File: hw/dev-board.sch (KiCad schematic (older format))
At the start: 8 parts

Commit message: Complete Header connections and internal U2-328 connections. Power regulation and misc passives are up next.
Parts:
- added 100n (x2), 1u: C, symbol C
- added 10K, 1K (x3), R? (x3): R, symbol R
- added D? (x2): LED, symbol LED
- added P?: CONN_02X03, symbol CONN_02X03
- added X?: RESONATOR, symbol RESONATOR
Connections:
- net labels added: +5V, AD0, AD1, AD2, AD3, AD4/SCL, AD4/SDA, AD5/SCL, AREF, IO0/RX, IO1/TX, IO2, IO3, IO4, IO5, IO6, IO7, IO8, IO9, MISO_328, MOSI_328, RES1, RES2, RST_328, RXLED, SCK_328, TXLED, UNUSED, ~SS~_328
- wire segments 5 -> 35
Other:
- moved on the sheet: P?

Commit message: Missing regulators. Xtal is fixed. 3.3v done. Power rails organized.
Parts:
- added C?: 100n, symbol C
- added C?: 470p, symbol C
- added C?: 1u, symbol C
- added CG0603MLC-05E, VR?: VR, symbol VR
- added F?: 500m, symbol F_Small
- added L?: Inductor, symbol L_Small
- added Q?: FDN340P, TO_SOT_Packages_SMD:SOT-23, symbol FDN340P
- added R? (x2): R, symbol R
- added U?: LM358, symbol LM358
- added U?: MIC5205, symbol MIC5205
- added X?: RESONATOR, symbol RESONATOR
- C?: renamed from 100n; value C -> 100n
- C?: renamed from 1u; value C -> 1u
- R?: renamed from 10K; value R -> 10K
- R?: value R -> 10K
- R?: renamed from 1K; value R -> 1K
- renumbered 1K to R?
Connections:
- net labels added: +3.3V, RES1_U2, RES2_U2, USBVCC, VIN
- wire segments 35 -> 59
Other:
- moved on the sheet: P?, R?, X?

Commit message: Add 5V regulator, clean up SOT-223 footprint, created 5V reg schematic symbol
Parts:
- added C?: 100n, symbol C
- added C?: 47u, symbol CP
- added R? (x2): 22R, symbol R
- added U?: LM2940LD-5.0, pcbfp_lib:SOT-223, symbol LM2940LD-5.0
- gave numbers to parts that had none: 1
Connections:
- net labels added: RES1_328, RES2_328
- net labels removed: RES1, RES2
- wire segments 59 -> 64
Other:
- moved on the sheet: C?, P?, Q?, R?, U?, U?A, X?

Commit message: Add schematic drawing of 328PB
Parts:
- added C? (x2): 15pf, symbol C
- added R?: 1M, symbol R
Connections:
- wire segments 64 -> 71
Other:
- moved on the sheet: C?, P?, Q?, R?, U?, U?A

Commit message: Added ATTINY85 schematic and SRAM schematic. Added T1's programming header. Up next, T1 needs a bus switch and everything needs to be duplcated for T2.
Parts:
- removed U?: ATMEGA328P-M, MLF/QFN32, symbol ATMEGA328P-M
- added IC?: ATMEGA328PB-MU, MLF/QFN32, symbol ATMEGA328PB-MU
- added IC?: ATTINY85-SUR, SO8-200, symbol ATTINY85-SUR
- added IC?: 23K256, SMD_Packages:SOIC-8-N, symbol 23K256
- added P? (x2): CONN_02X03, symbol CONN_02X03
- added R?: 10K, symbol R
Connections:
- net labels added: IO3_T1, IO4_T1, MISO_T1, MOSI_T1, SCK_T1, ~RST~_T1
- wire segments 71 -> 80
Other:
- moved on the sheet: C?, P?, R?, X?

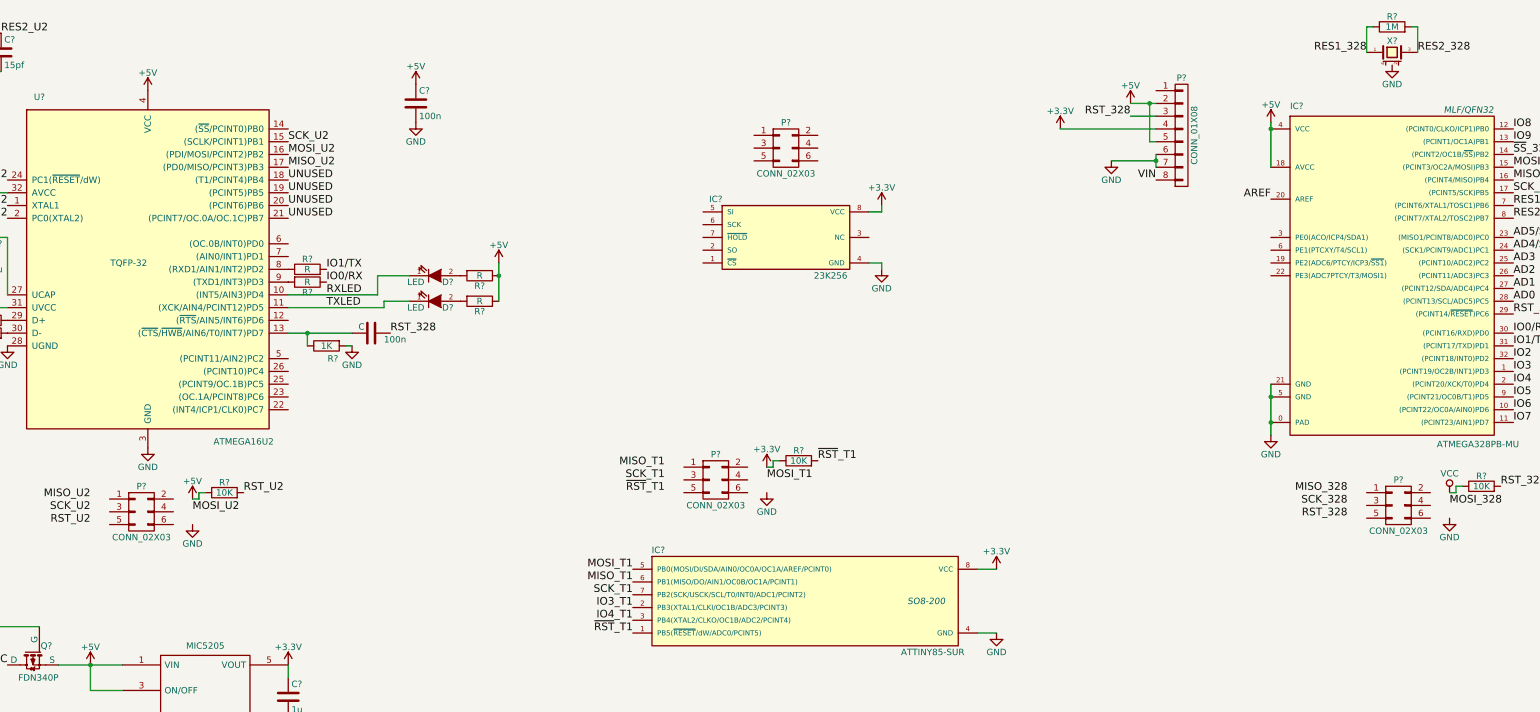
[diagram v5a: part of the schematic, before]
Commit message: Added Bus switch schematic, added a mosfet for power to ram and bs. Needed for programming. BS and ram are not 5v tolerant.
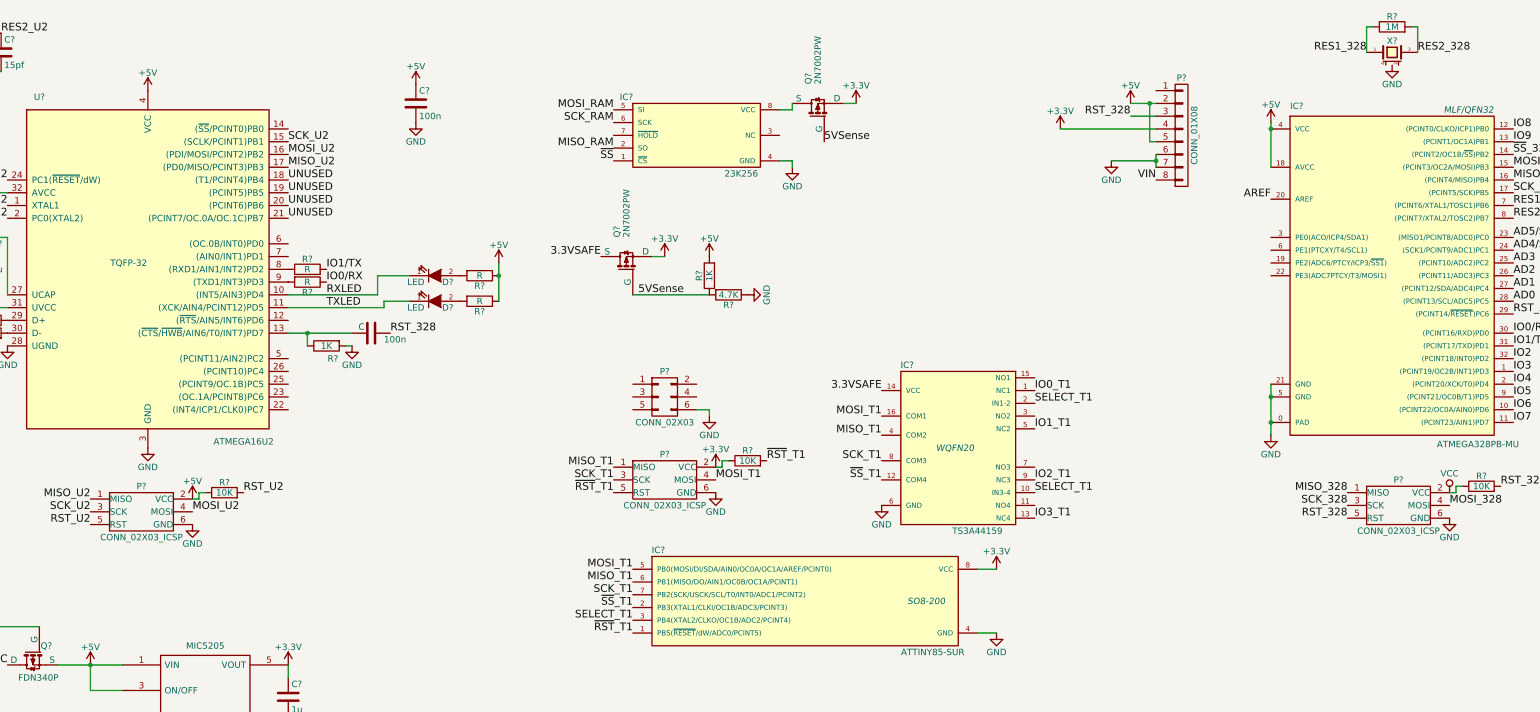
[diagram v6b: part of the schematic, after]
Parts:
- removed P? (x4): CONN_02X03, symbol CONN_02X03
- added IC?: TS3A44159, WQFN20, symbol TS3A44159
- added P? (x3): CONN_02X03_ICSP, symbol CONN_02X03_ICSP
- added P?: CONN_02X03, symbol CONN_02X03
- added Q? (x2): 2N7002PW, TO_SOT_Packages_SMD:SOT-23, symbol 2N7002PW
- added R?: 1K, symbol R
- added R?: 4.7K, symbol R
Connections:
- net +3V3: now also P?.2 (VCC), Q?.~ (S), Q?.~ (S); no longer IC?.8 (VCC)
- net +5V: now also P?.2 (VCC), R?.2
- net GND: now also IC?.6 (GND), P?.6 (GND), P?.6 (GND), P?.6 (GND), P?.6 (P6), R?.1
- net IO3_T1: now also IC?.13 (NC4); no longer IC?.2 (PB3(XTAL1/CLKI/OC1B/ADC3/PCINT3))
- net MISO_328: now also P?.1 (MISO)
- net MISO_T1: now also IC?.4 (COM2), P?.1 (MISO)
- net MISO_U2: now also P?.1 (MISO)
- net MOSI_328: now also P?.4 (MOSI)
- net MOSI_T1: now also IC?.16 (COM1), P?.4 (MOSI)
- net MOSI_U2: now also P?.4 (MOSI)
- net RST_328: now also P?.5 (RST)
- net RST_U2: now also P?.5 (RST)
- net SCK_328: now also P?.3 (SCK)
- net SCK_T1: now also IC?.8 (COM3), P?.3 (SCK)
- net SCK_U2: now also P?.3 (SCK)
- net VCC: now also P?.2 (VCC)
- net ~RST~_T1: now also P?.5 (RST)
- net ~SS~: now reaches IC?.1 (~CS)
- net MISO_RAM: now reaches IC?.2 (SO)
- net MOSI_RAM: now reaches IC?.5 (SI)
- net SCK_RAM: now reaches IC?.6 (SCK)
- net IO4_T1 renamed SELECT_T1
- net SELECT_T1: now also IC?.10 (IN3-4), IC?.2 (IN1-2)
- new net: IC?.8 (VCC), Q?.~ (S)
- new net 3.3VSAFE: IC?.14 (VCC), Q?.~ (S)
- new net 5VSense: Q?.~ (S), Q?.~ (S), R?.1, R?.2
- new net IO0_T1: IC?.1 (NC1)
- new net IO1_T1: IC?.5 (NC2)
- new net IO2_T1: IC?.9 (NC3)
- new net ~SS~_T1: IC?.12 (COM4), IC?.2 (PB3(XTAL1/CLKI/OC1B/ADC3/PCINT3))
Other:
- moved on the sheet: IC?, R?

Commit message: Switched Safe 3.3v rail for an unsafe rail. This keeps power management less complicated.
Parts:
- removed Q?: 2N7002PW, TO_SOT_Packages_SMD:SOT-23, symbol 2N7002PW
- added CON?: BARREL_JACK, symbol BARREL_JACK
- added D?: D, symbol D
- added D?: LED, symbol LED
- added IC?: ATTINY85-SUR, SO8-200, symbol ATTINY85-SUR
- added IC?: TS3A44159, WQFN20, symbol TS3A44159
- added P?: CONN_02X03_ICSP, symbol CONN_02X03_ICSP
- added P?: CONN_02X03, symbol CONN_02X03
- added Q?: 2N7002PW, TO_SOT_Packages_SMD:SOT-23, symbol 2N7002PW
- added R? (x3): 10K, symbol R
- added R?: 1K, symbol R
- R? (x2): value R -> 1K
- R? (x2): value R -> 10K
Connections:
- net 3.3VSAFE is gone; now on net +3V3: IC?.14 (VCC)
- net +3V3: now also IC?.7 (~HOLD), IC?.8 (VCC), P?.2 (P2), IC?.14 (VCC), P?.2 (P2), P?.2 (VCC), Q?.~ (S), R?.1; no longer IC?.8 (VCC)
- net +5V: now also R?.1
- net 5VSense: now also Q?.~ (S)
- net GND: now also CON?.2, CON?.3, IC?.4 (GND), IC?.6 (GND), P?.6 (GND), P?.6 (P6), R?.1, R?.1
- net IO0_T1: now also P?.1 (P1)
- net IO1_T1: now also P?.3 (P3)
- net IO2_T1: now also P?.5 (P5)
- net IO3_T1: now also P?.4 (P4)
- net MISO_RAM: now also IC?.3 (NO2), IC?.3 (NO2)
- net MOSI_RAM: now also IC?.15 (NO1), IC?.15 (NO1)
- net SCK_RAM: now also IC?.7 (NO3), IC?.7 (NO3)
- net SELECT_T1: now also R?.2
- net VIN: now also D?.1 (K)
- net ~SS~: now also IC?.11 (NO4), IC?.11 (NO4)
- net at U?.22 ((INT4/ICP1/CLK0)PC7): now also D?.1 (K)
- new net: CON?.1, D?.2 (A)
- new net: D?.2 (A), R?.2
- new net 3.3V_UNSAFE: IC?.8 (VCC), IC?.8 (VCC), Q?.~ (S), Q?.~ (S)
- new net IO0_T2: IC?.1 (NC1), P?.1 (P1)
- new net IO1_T2: IC?.5 (NC2), P?.3 (P3)
- new net IO2_T2: IC?.9 (NC3), P?.5 (P5)
- new net IO3_T2: IC?.13 (NC4), P?.4 (P4)
- new net MISO_T2: IC?.4 (COM2), IC?.6 (PB1(MISO/DO/AIN1/OC0B/OC1A/PCINT1)), P?.1 (MISO)
- new net MOSI_T2: IC?.16 (COM1), IC?.5 (PB0(MOSI/DI/SDA/AIN0/OC0A/OC1A/AREF/PCINT0)), P?.4 (MOSI)
- new net SCK_T2: IC?.7 (PB2(SCK/USCK/SCL/T0/INT0/ADC1/PCINT2)), IC?.8 (COM3), P?.3 (SCK)
- new net SELECT_T2: IC?.10 (IN3-4), IC?.2 (IN1-2), IC?.3 (PB4(XTAL2/CLKO/OC1B/ADC2/PCINT4)), R?.2
- new net ~RST~_T2: IC?.1 (PB5(~RESET~/dW/ADC0/PCINT5)), P?.5 (RST), R?.2
- new net ~SS~_T2: IC?.12 (COM4), IC?.2 (PB3(XTAL1/CLKI/OC1B/ADC3/PCINT3))
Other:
- moved on the sheet: 100n, C?, CG0603MLC-05E, D?, F?, IC?, L?, P?, Q?, R?, U?, U?A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

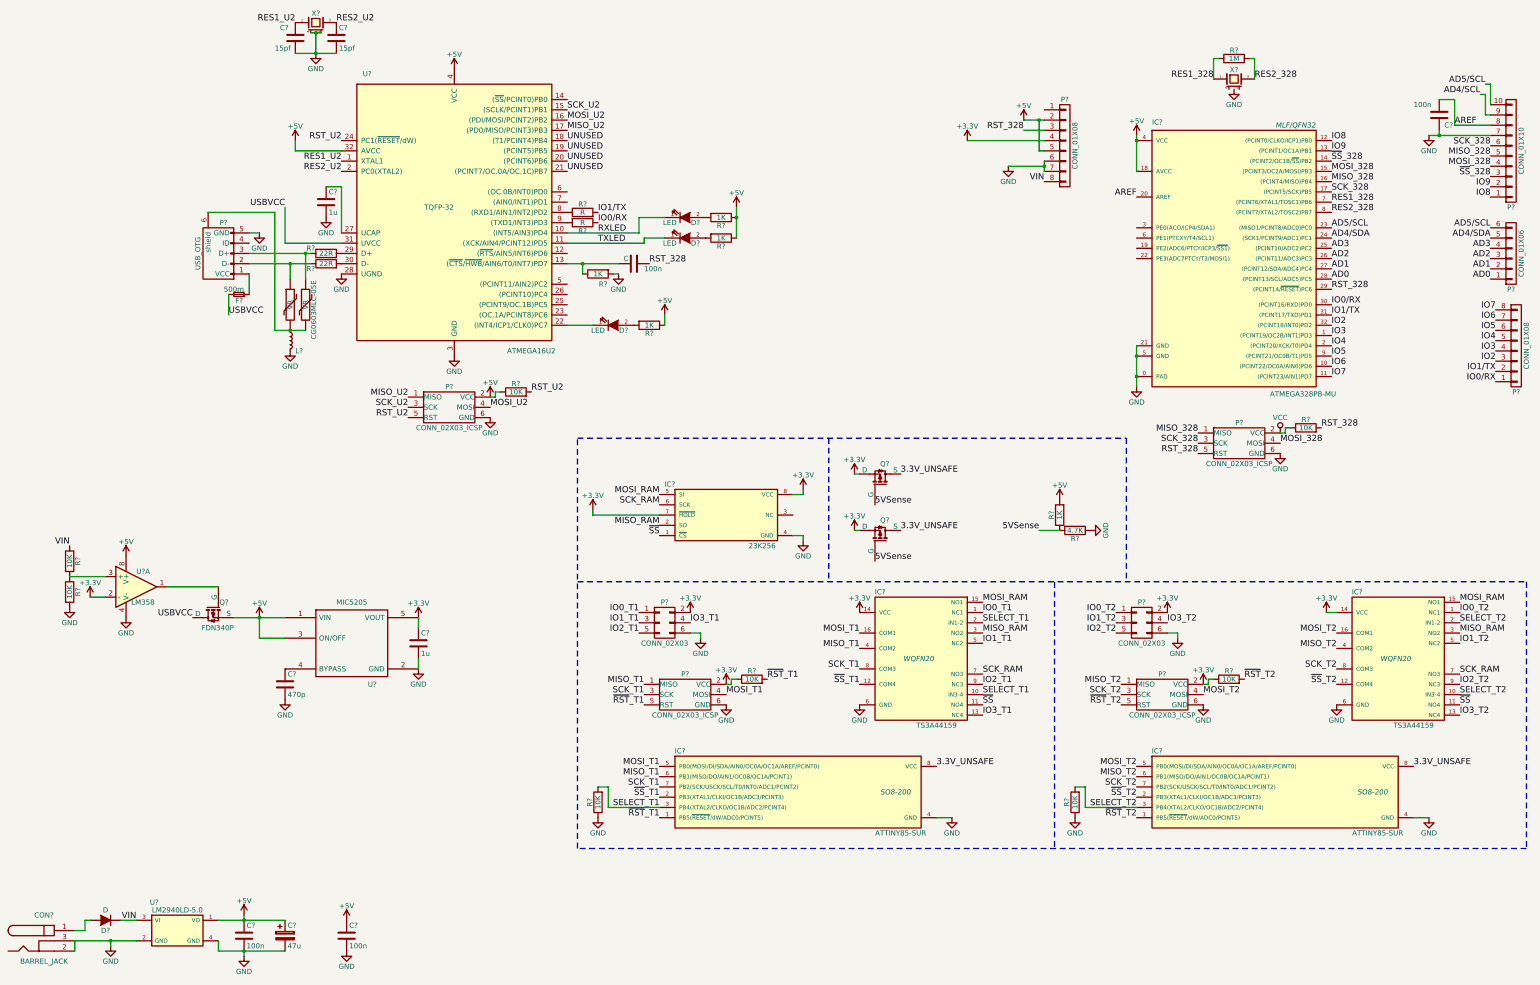
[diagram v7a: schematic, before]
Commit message: Okay, the Schematic really is done now. Added a level shifter on 328<->SRAM
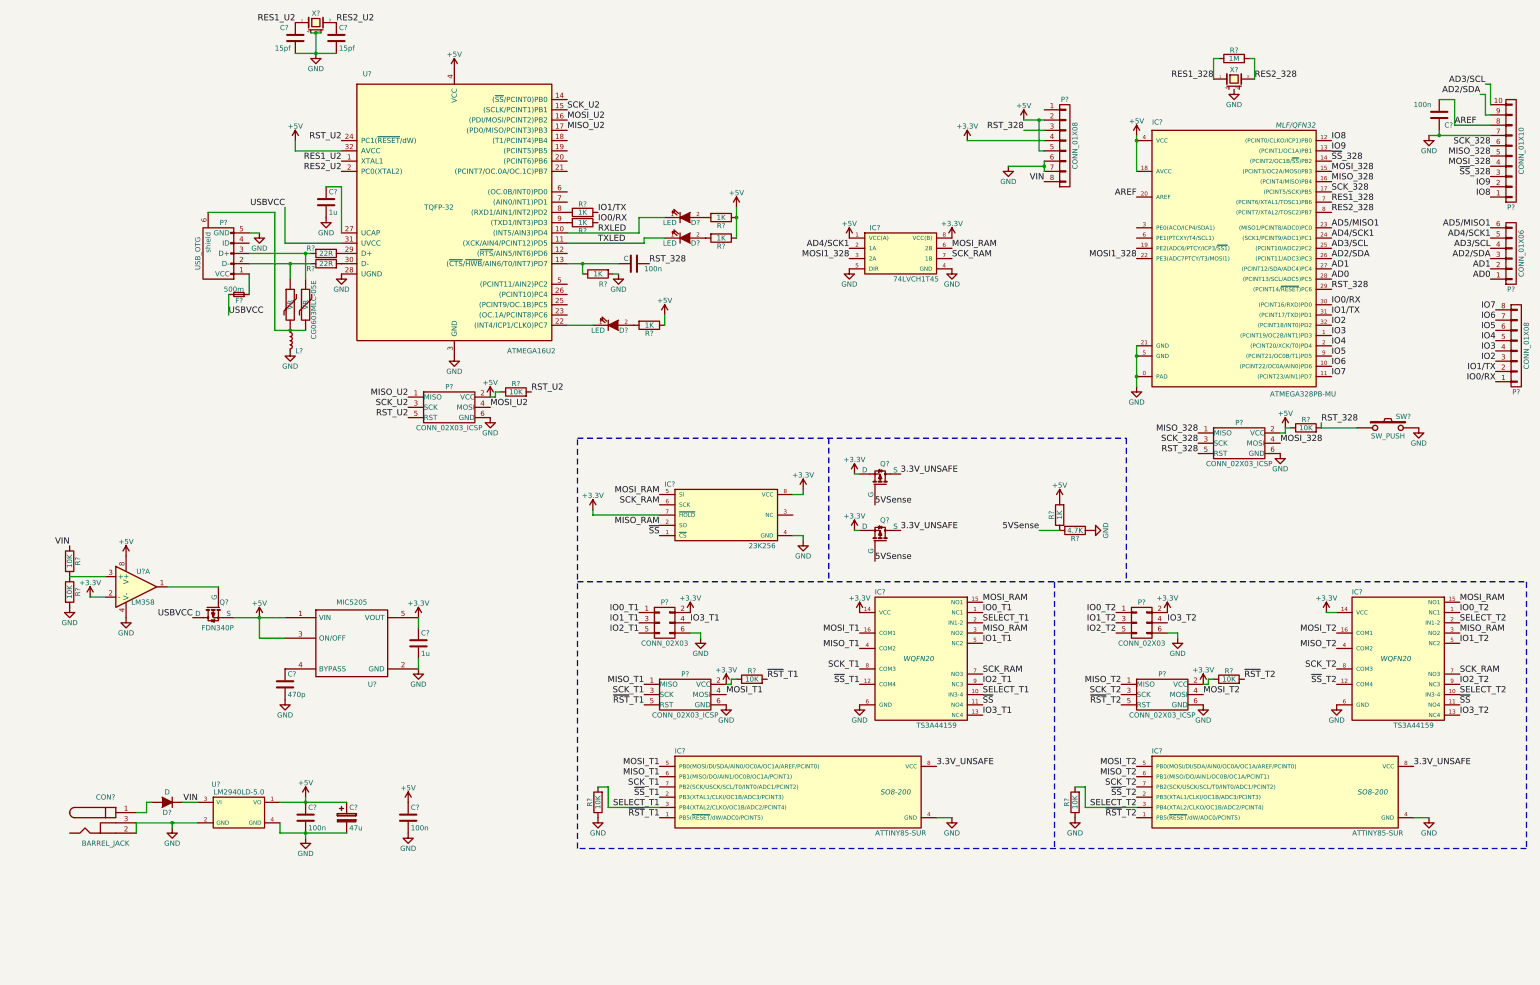
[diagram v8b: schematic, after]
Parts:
- added IC?: 74LVCH1T45, TO_SOT_Packages_SMD:SOT-886, symbol 74LVCH1T45
- added SW?: SW_PUSH, symbol SW_PUSH
- R? (x2): value R -> 1K
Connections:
- net AD4/SCL is gone; now on net AD2/SDA: P?.9 (P9)
- net VCC is gone; now on net +5V: P?.2 (VCC), R?.1
- net +3V3: now also IC?.8 (VCC(B))
- net +5V: now also IC?.1 (VCC(A))
- net GND: now also IC?.4 (GND), IC?.5 (DIR), SW?.2
- net MOSI_RAM: now also IC?.6 (2B)
- net RST_328: now also SW?.1
- net SCK_RAM: now also IC?.7 (1B)
- net MOSI1_328: now reaches IC?.22 (PE3(ADC7PTCY/T3/MOSI1))
- net MOSI1_328: now also IC?.3 (2A)
- net AD2 renamed AD2/SDA
- net AD3 renamed AD3/SCL
- net AD3/SCL: now also P?.10 (P10)
- net AD4/SDA renamed AD4/SCK1
- net AD4/SCK1: now also IC?.2 (1A)
- net AD5/SCL renamed AD5/MISO1
- net AD5/MISO1: no longer P?.10 (P10)
- removed net UNUSED: U?.18 ((T1/PCINT4)PB4), U?.19 ((PCINT5)PB5), U?.20 ((PCINT6)PB6), U?.21 ((PCINT7/OC.0A/OC.1C)PB7)
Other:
- moved on the sheet: C?, CON?, D?, U?
